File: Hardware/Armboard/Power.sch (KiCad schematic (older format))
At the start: 13 parts, among them J1 Test_Point, U1 LM2576D2TR4

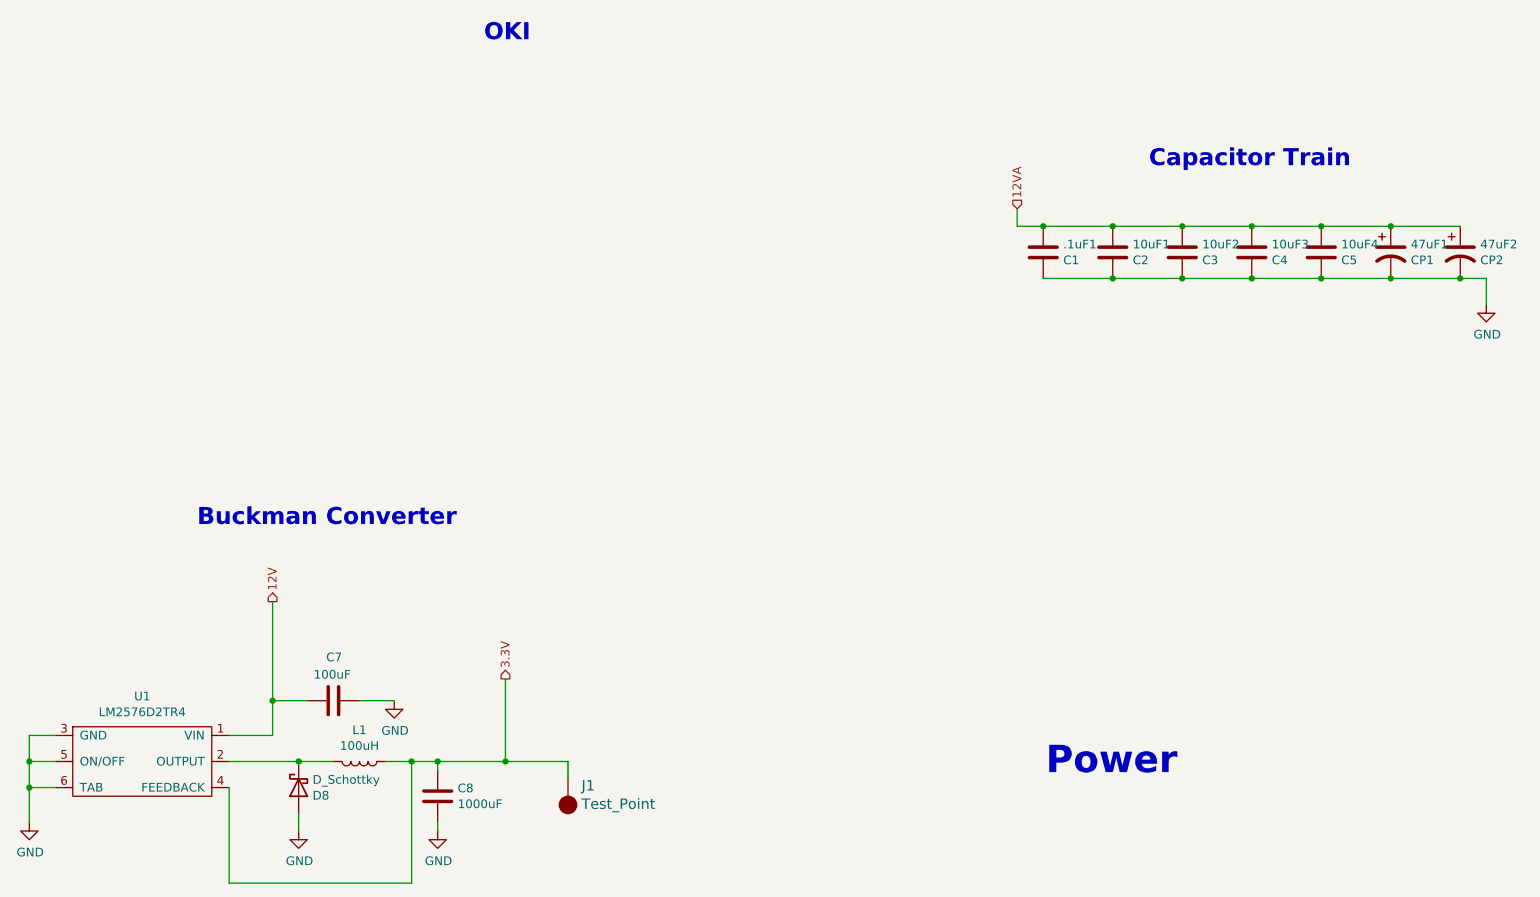
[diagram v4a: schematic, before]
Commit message: Replaced buckman with OKI
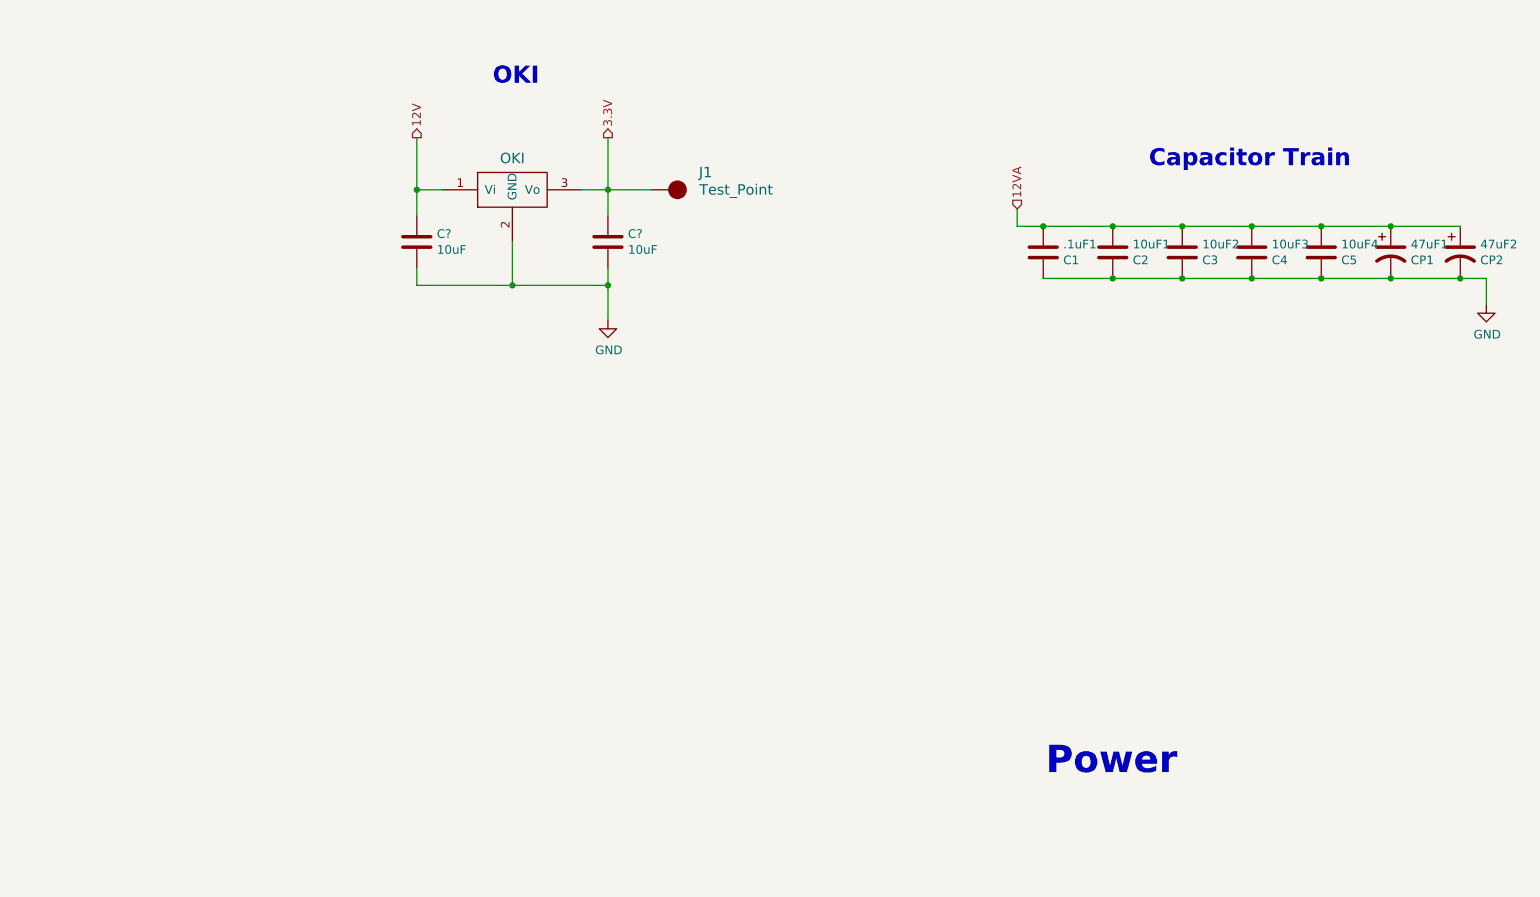
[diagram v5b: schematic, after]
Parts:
- removed C7: 100uF, Capacitor_SMD:C_0603_1608Metric_Pad1.05x0.95mm_HandSolder, symbol Device:C
- removed C8: 1000uF, Capacitor_SMD:C_0603_1608Metric_Pad1.05x0.95mm_HandSolder, symbol Device:C
- removed D8: D_Schottky, Diode_THT:D_DO-201AD_P15.24mm_Horizontal, symbol Device:D_Schottky
- removed L1: 100uH, Inductor_SMD:L_0603_1608Metric_Pad1.05x0.95mm_HandSolder, symbol Device:L
- removed U1: LM2576D2TR4, MRDT_Devices:LM2576, symbol Armboard-rescue:LM2576D2TR4-MRDT_Devices-Armboard-rescue
- added C? (x2): 10uF, symbol Device:C
- added U?: OKI, symbol MRDT_Devices:OKI
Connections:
- net 12V: now also C?.1, U?.1 (Vi)
- net 3.3V: now also C?.1, U?.3 (Vo)
- net GND: now also C?.2, C?.2, U?.2 (GND)
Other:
- note removed: "Buckman Converter"
- moved on the sheet: J1
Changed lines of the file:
@@
 $EndComp
 $Comp
-L Armboard-rescue:LM2576D2TR4-MRDT_Devices-Armboard-rescue U1
-U 1 1 5F74DE4A
-P 1420 7090
-F 0 "U1" H 1420 7515 50  0000 C CNN
-F 1 "LM2576D2TR4" H 1420 7424 50  0000 C CNN
-F 2 "MRDT_Devices:LM2576" H 1420 7540 50  0001 C CNN
-F 3 "https://www.mouser.com/datasheet/2/308/LM2576_D-1810688.pdf" H 1420 7540 50  0001 C CNN
-	1    1420 7090
+L Armboard-rescue:Test_Point-MRDT_Connectors-Armboard-rescue J1
+U 1 1 5F75C39D
+P 4350 3750
+F 0 "J1" V 4250 4100 60  0000 R CNN
+F 1 "Test_Point" V 4350 4450 60  0000 R CNN
+F 2 "TestPoint:TestPoint_Pad_D2.5mm" H 4350 3700 60  0001 C CNN
+F 3 "" H 4350 3700 60  0001 C CNN
+	1    4350 3750
+	0    1    1    0
+$EndComp
+Text Notes 8375 3630 2    98   ~ 20
+Capacitor Train
+Text Notes 6620 7130 0    157  ~ 31
+Power
+Text HLabel 4100 3450 1    50   Output ~ 0
+3.3V
+Text HLabel 3000 3450 1    50   Output ~ 0
+12V
+Text HLabel 6455 3860 1    50   Input ~ 0
+12VA
+Text Notes 3705 3155 2    98   ~ 20
+OKI
+$Comp
+L MRDT_Devices:OKI U?
+U 1 1 5FB74CE4
+P 3350 3850
+F 0 "U?" H 3400 3800 60  0001 C CNN
+F 1 "OKI" H 3550 4131 60  0000 C CNN
+F 2 "" H 3150 3750 60  0001 C CNN
+F 3 "" H 3150 3750 60  0001 C CNN
+	1    3350 3850
 	1    0    0    -1
 $EndComp
 $Comp
-L power:GND #PWR08
-U 1 1 5F74E2A1
-P 770 7390
-F 0 "#PWR08" H 770 7140 50  0001 C CNN
-F 1 "GND" H 775 7217 50  0000 C CNN
-F 2 "" H 770 7390 50  0001 C CNN
-F 3 "" H 770 7390 50  0001 C CNN
-	1    770  7390
+L Device:C C?
+U 1 1 5FB77225
+P 3000 4050
+F 0 "C?" H 3115 4096 50  0000 L CNN
+F 1 "10uF" H 3115 4005 50  0000 L CNN
+F 2 "" H 3038 3900 50  0001 C CNN
+F 3 "~" H 3000 4050 50  0001 C CNN
+	1    3000 4050
+	1    0    0    -1
+$EndComp
+$Comp
+L Device:C C?
+U 1 1 5FB780BA
+P 4100 4050
+F 0 "C?" H 4215 4096 50  0000 L CNN
+F 1 "10uF" H 4215 4005 50  0000 L CNN
+F 2 "" H 4138 3900 50  0001 C CNN
+F 3 "~" H 4100 4050 50  0001 C CNN
+	1    4100 4050
+	1    0    0    -1
+$EndComp
+$Comp
+L power:GND #PWR?
+U 1 1 5FB785A8
+P 4100 4500
+F 0 "#PWR?" H 4100 4250 50  0001 C CNN
+F 1 "GND" H 4105 4327 50  0000 C CNN
+F 2 "" H 4100 4500 50  0001 C CNN
+F 3 "" H 4100 4500 50  0001 C CNN
+	1    4100 4500
 	1    0    0    -1
 $EndComp
 Wire Wire Line
-	920  6890 770  6890
+	3000 4200 3000 4300
 Wire Wire Line
-	920  7040 770  7040
+	3000 4300 3550 4300
 Wire Wire Line
-	770  6890 770  7040
-Connection ~ 770  7040
+	4100 4300 4100 4200
+Connection ~ 4100 4300
 Wire Wire Line
-	920  7190 770  7190
+	4100 4300 4100 4500
 Wire Wire Line
-	770  7040 770  7190
-Connection ~ 770  7190
+	3000 3900 3000 3750
 Wire Wire Line
-	770  7190 770  7390
+	3000 3750 3150 3750
 Wire Wire Line
-	1920 6890 2170 6890
+	3550 4050 3550 4300
+Connection ~ 3550 4300
 Wire Wire Line
-	2170 6890 2170 6690
-$Comp
-L Device:C C8
-U 1 1 5F750C41
-P 3120 7240
-F 0 "C8" H 3235 7286 50  0000 L CNN
-F 1 "1000uF" H 3235 7195 50  0000 L CNN
-F 2 "Capacitor_SMD:C_0603_1608Metric_Pad1.05x0.95mm_HandSolder" H 3158 7090 50  0001 C CNN
-F 3 "~" H 3120 7240 50  0001 C CNN
-	1    3120 7240
-	1    0    0    -1
-$EndComp
-$Comp
-L Device:C C7
-U 1 1 5F75145E
-P 2520 6690
-F 0 "C7" V 2770 6640 50  0000 L CNN
-F 1 "100uF" V 2670 6590 50  0000 L CNN
-F 2 "Capacitor_SMD:C_0603_1608Metric_Pad1.05x0.95mm_HandSolder" H 2558 6540 50  0001 C CNN
-F 3 "~" H 2520 6690 50  0001 C CNN
-	1    2520 6690
-	0    -1   -1   0
-$EndComp
+	3550 4300 4100 4300
 Wire Wire Line
-	2170 6690 2370 6690
-Connection ~ 2170 6690
-$Comp
-L power:GND #PWR010
-U 1 1 5F75423C
-P 2870 6690
-F 0 "#PWR010" H 2870 6440 50  0001 C CNN
-F 1 "GND" H 2875 6517 50  0000 C CNN
-F 2 "" H 2870 6690 50  0001 C CNN
-F 3 "" H 2870 6690 50  0001 C CNN
-	1    2870 6690
-	1    0    0    -1
-$EndComp
+	4100 3750 4100 3900
 Wire Wire Line
-	2670 6690 2870 6690
-$Comp
-L Device:L L1
-U 1 1 5F755388
-P 2670 7040
-F 0 "L1" V 2489 7040 50  0000 C CNN
-F 1 "100uH" V 2580 7040 50  0000 C CNN
-F 2 "Inductor_SMD:L_0603_1608Metric_Pad1.05x0.95mm_HandSolder" H 2670 7040 50  0001 C CNN
-F 3 "~" H 2670 7040 50  0001 C CNN
-	1    2670 7040
-	0    1    1    0
-$EndComp
-$Comp
-L power:GND #PWR09
-U 1 1 5F75782E
-P 2320 7440
-F 0 "#PWR09" H 2320 7190 50  0001 C CNN
-F 1 "GND" H 2325 7267 50  0000 C CNN
-F 2 "" H 2320 7440 50  0001 C CNN
-F 3 "" H 2320 7440 50  0001 C CNN
-	1    2320 7440
-	1    0    0    -1
-$EndComp
+	3950 3750 4100 3750
 Wire Wire Line
-	2320 7340 2320 7440
+	3000 3750 3000 3450
+Connection ~ 3000 3750
 Wire Wire Line
-	2820 7040 2970 7040
+	4100 3750 4100 3450
+Connection ~ 4100 3750
 Wire Wire Line
-	3120 7040 3120 7090
-Wire Wire Line
-	1920 7190 1920 7740
-Wire Wire Line
-	1920 7740 2970 7740
-Wire Wire Line
-	2970 7740 2970 7040
-Connection ~ 2970 7040
-Wire Wire Line
-	2970 7040 3120 7040
-$Comp
-L power:GND #PWR011
-U 1 1 5F75A24F
-P 3120 7440
-F 0 "#PWR011" H 3120 7190 50  0001 C CNN
-F 1 "GND" H 3125 7267 50  0000 C CNN
-F 2 "" H 3120 7440 50  0001 C CNN
-F 3 "" H 3120 7440 50  0001 C CNN
-	1    3120 7440
-	1    0    0    -1
-$EndComp
-Wire Wire Line
-	3120 7440 3120 7390
-$Comp
-L Armboard-rescue:Test_Point-MRDT_Connectors-Armboard-rescue J1
-U 1 1 5F75C39D
-P 3870 7140
-F 0 "J1" H 3792 7179 60  0000 R CNN
-F 1 "Test_Point" H 3792 7285 60  0000 R CNN
-F 2 "TestPoint:TestPoint_Pad_D2.5mm" H 3870 7090 60  0001 C CNN
-F 3 "" H 3870 7090 60  0001 C CNN
-	1    3870 7140
-	-1   0    0    1
-$EndComp
-Wire Wire Line
-	3870 7040 3870 7140
-Connection ~ 3120 7040
-Text Notes 3230 5695 2    98   ~ 20
-Buckman Converter
-Text Notes 8375 3630 2    98   ~ 20
-Capacitor Train
-$Comp
-L Device:D_Schottky D8
-U 1 1 5F83C9A2
-P 2320 7190
-F 0 "D8" V 2366 7110 50  0000 R CNN
-F 1 "D_Schottky" V 2275 7110 50  0000 R CNN
-F 2 "Diode_THT:D_DO-201AD_P15.24mm_Horizontal" H 2320 7190 50  0001 C CNN
-F 3 "~" H 2320 7190 50  0001 C CNN
-	1    2320 7190
-	0    -1   1    0
-$EndComp
-Wire Wire Line
-	1920 7040 2320 7040
-Connection ~ 2320 7040
-Wire Wire Line
-	2320 7040 2520 7040
-Text Notes 6620 7130 0    157  ~ 31
-Power
-Text HLabel 3510 6565 1    50   Output ~ 0
-3.3V
-Text HLabel 2170 6120 1    50   Output ~ 0
-12V
-Wire Wire Line
-	2170 6120 2170 6690
-Wire Wire Line
-	3120 7040 3510 7040
-Wire Wire Line
-	3510 6565 3510 7040
-Connection ~ 3510 7040
-Wire Wire Line
-	3510 7040 3870 7040
-Text HLabel 6455 3860 1    50   Input ~ 0
-12VA
-Text Notes 3655 2905 2    98   ~ 20
-OKI
+	4100 3750 4350 3750
 $EndSCHEMATC

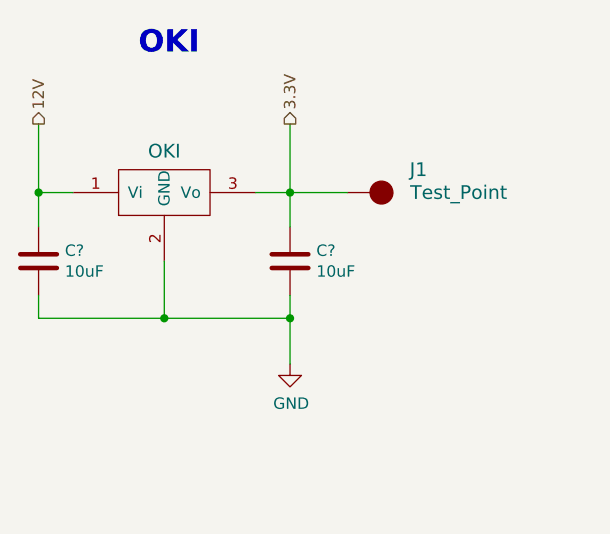
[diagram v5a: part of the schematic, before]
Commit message: Updated footprints, generated new netlist
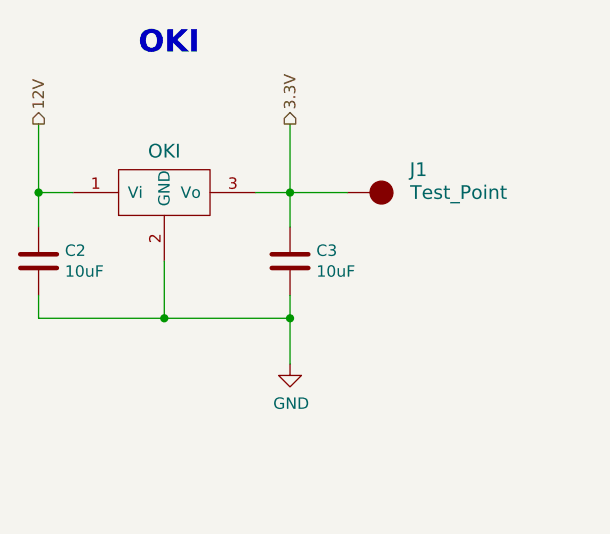
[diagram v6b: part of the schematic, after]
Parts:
- C2, C3: renamed from C?; footprint (none) -> Capacitor_SMD:C_0603_1608Metric_Pad1.05x0.95mm_HandSolder
- J1: footprint TestPoint:TestPoint_Pad_D2.5mm -> TestPoint:TestPoint_Pad_3.0x3.0mm
- U1: renamed from U?; footprint (none) -> MRDT_Devices:OKI_Horizontal
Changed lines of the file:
@@
 F 0 "J1" V 4250 4100 60  0000 R CNN
 F 1 "Test_Point" V 4350 4450 60  0000 R CNN
-F 2 "TestPoint:TestPoint_Pad_D2.5mm" H 4350 3700 60  0001 C CNN
+F 2 "TestPoint:TestPoint_Pad_3.0x3.0mm" H 4350 3700 60  0001 C CNN
 F 3 "" H 4350 3700 60  0001 C CNN
 	1    4350 3750
@@
 OKI
 $Comp
-L MRDT_Devices:OKI U?
+L MRDT_Devices:OKI U1
 U 1 1 5FB74CE4
 P 3350 3850
-F 0 "U?" H 3400 3800 60  0001 C CNN
+F 0 "U1" H 3400 3800 60  0001 C CNN
 F 1 "OKI" H 3550 4131 60  0000 C CNN
-F 2 "" H 3150 3750 60  0001 C CNN
+F 2 "MRDT_Devices:OKI_Horizontal" H 3150 3750 60  0001 C CNN
 F 3 "" H 3150 3750 60  0001 C CNN
 	1    3350 3850
@@
 $EndComp
 $Comp
-L Device:C C?
+L Device:C C2
 U 1 1 5FB77225
 P 3000 4050
-F 0 "C?" H 3115 4096 50  0000 L CNN
+F 0 "C2" H 3115 4096 50  0000 L CNN
 F 1 "10uF" H 3115 4005 50  0000 L CNN
-F 2 "" H 3038 3900 50  0001 C CNN
+F 2 "Capacitor_SMD:C_0603_1608Metric_Pad1.05x0.95mm_HandSolder" H 3038 3900 50  0001 C CNN
 F 3 "~" H 3000 4050 50  0001 C CNN
 	1    3000 4050
@@
 $EndComp
 $Comp
-L Device:C C?
+L Device:C C3
 U 1 1 5FB780BA
 P 4100 4050
-F 0 "C?" H 4215 4096 50  0000 L CNN
+F 0 "C3" H 4215 4096 50  0000 L CNN
 F 1 "10uF" H 4215 4005 50  0000 L CNN
-F 2 "" H 4138 3900 50  0001 C CNN
+F 2 "Capacitor_SMD:C_0603_1608Metric_Pad1.05x0.95mm_HandSolder" H 4138 3900 50  0001 C CNN
 F 3 "~" H 4100 4050 50  0001 C CNN
 	1    4100 4050
@@
 $EndComp
 $Comp
-L power:GND #PWR?
+L power:GND #PWR01
 U 1 1 5FB785A8
 P 4100 4500
-F 0 "#PWR?" H 4100 4250 50  0001 C CNN
+F 0 "#PWR01" H 4100 4250 50  0001 C CNN
 F 1 "GND" H 4105 4327 50  0000 C CNN
 F 2 "" H 4100 4500 50  0001 C CNN

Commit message: Added silkscreen designs
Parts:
- 47uF1, 47uF2: footprint Capacitor_SMD:CP_Elec_5x5.4 -> Capacitor_THT:CP_Radial_D5.0mm_P2.50mm
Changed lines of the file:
@@
 F 0 "47uF1" H 8720 4156 50  0000 L CNN
 F 1 "CP1" H 8720 4065 50  0000 L CNN
-F 2 "Capacitor_SMD:CP_Elec_5x5.4" H 8605 4110 50  0001 C CNN
+F 2 "Capacitor_THT:CP_Radial_D5.0mm_P2.50mm" H 8605 4110 50  0001 C CNN
 F 3 "~" H 8605 4110 50  0001 C CNN
 	1    8605 4110
@@
 F 0 "47uF2" H 9120 4156 50  0000 L CNN
 F 1 "CP2" H 9120 4065 50  0000 L CNN
-F 2 "Capacitor_SMD:CP_Elec_5x5.4" H 9005 4110 50  0001 C CNN
+F 2 "Capacitor_THT:CP_Radial_D5.0mm_P2.50mm" H 9005 4110 50  0001 C CNN
 F 3 "~" H 9005 4110 50  0001 C CNN
 	1    9005 4110

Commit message: Fixed some library issues and moved Gerbs to Manufacturing folder
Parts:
- .1uF1, 10uF1, 10uF2, 10uF3, 10uF4, C2, C3: footprint Capacitor_SMD:C_0603_1608Metric_Pad1.05x0.95mm_HandSolder -> Capacitor_SMD:C_0603_1608Metric_Pad1.08x0.95mm_HandSolder
- 47uF1, 47uF2: symbol Device:CP1 -> Device:C_Polarized_US
- J1: symbol Armboard-rescue:Test_Point-MRDT_Connectors-Armboard-rescue -> MRDT_Connectors:Test_Point
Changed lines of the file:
@@
 EESchema Schematic File Version 4
+LIBS:Armboard-cache
 EELAYER 30 0
 EELAYER END
@@
 F 0 ".1uF1" H 6720 4156 50  0000 L CNN
 F 1 "C1" H 6720 4065 50  0000 L CNN
-F 2 "Capacitor_SMD:C_0603_1608Metric_Pad1.05x0.95mm_HandSolder" H 6643 3960 50  0001 C CNN
+F 2 "Capacitor_SMD:C_0603_1608Metric_Pad1.08x0.95mm_HandSolder" H 6643 3960 50  0001 C CNN
 F 3 "~" H 6605 4110 50  0001 C CNN
 	1    6605 4110
@@
 F 0 "10uF1" H 7120 4156 50  0000 L CNN
 F 1 "C2" H 7120 4065 50  0000 L CNN
-F 2 "Capacitor_SMD:C_0603_1608Metric_Pad1.05x0.95mm_HandSolder" H 7043 3960 50  0001 C CNN
+F 2 "Capacitor_SMD:C_0603_1608Metric_Pad1.08x0.95mm_HandSolder" H 7043 3960 50  0001 C CNN
 F 3 "~" H 7005 4110 50  0001 C CNN
 	1    7005 4110
@@
 F 0 "10uF2" H 7520 4156 50  0000 L CNN
 F 1 "C3" H 7520 4065 50  0000 L CNN
-F 2 "Capacitor_SMD:C_0603_1608Metric_Pad1.05x0.95mm_HandSolder" H 7443 3960 50  0001 C CNN
+F 2 "Capacitor_SMD:C_0603_1608Metric_Pad1.08x0.95mm_HandSolder" H 7443 3960 50  0001 C CNN
 F 3 "~" H 7405 4110 50  0001 C CNN
 	1    7405 4110
@@
 F 0 "10uF3" H 7920 4156 50  0000 L CNN
 F 1 "C4" H 7920 4065 50  0000 L CNN
-F 2 "Capacitor_SMD:C_0603_1608Metric_Pad1.05x0.95mm_HandSolder" H 7843 3960 50  0001 C CNN
+F 2 "Capacitor_SMD:C_0603_1608Metric_Pad1.08x0.95mm_HandSolder" H 7843 3960 50  0001 C CNN
 F 3 "~" H 7805 4110 50  0001 C CNN
 	1    7805 4110
@@
 F 0 "10uF4" H 8320 4156 50  0000 L CNN
 F 1 "C5" H 8320 4065 50  0000 L CNN
-F 2 "Capacitor_SMD:C_0603_1608Metric_Pad1.05x0.95mm_HandSolder" H 8243 3960 50  0001 C CNN
+F 2 "Capacitor_SMD:C_0603_1608Metric_Pad1.08x0.95mm_HandSolder" H 8243 3960 50  0001 C CNN
 F 3 "~" H 8205 4110 50  0001 C CNN
 	1    8205 4110
-	1    0    0    -1
-$EndComp
-$Comp
-L Device:CP1 47uF1
-U 1 1 5F67C954
-P 8605 4110
-F 0 "47uF1" H 8720 4156 50  0000 L CNN
-F 1 "CP1" H 8720 4065 50  0000 L CNN
-F 2 "Capacitor_THT:CP_Radial_D5.0mm_P2.50mm" H 8605 4110 50  0001 C CNN
-F 3 "~" H 8605 4110 50  0001 C CNN
-	1    8605 4110
-	1    0    0    -1
-$EndComp
-$Comp
-L Device:CP1 47uF2
-U 1 1 5F67D4A0
-P 9005 4110
-F 0 "47uF2" H 9120 4156 50  0000 L CNN
-F 1 "CP2" H 9120 4065 50  0000 L CNN
-F 2 "Capacitor_THT:CP_Radial_D5.0mm_P2.50mm" H 9005 4110 50  0001 C CNN
-F 3 "~" H 9005 4110 50  0001 C CNN
-	1    9005 4110
 	1    0    0    -1
 $EndComp
@@
 $EndComp
 $Comp
-L Armboard-rescue:Test_Point-MRDT_Connectors-Armboard-rescue J1
+L MRDT_Connectors:Test_Point J1
 U 1 1 5F75C39D
 P 4350 3750
+AR Path="/5F75C39D" Ref="J1"  Part="1"
+AR Path="/5F67ABAC/5F75C39D" Ref="J1"  Part="1"
 F 0 "J1" V 4250 4100 60  0000 R CNN
 F 1 "Test_Point" V 4350 4450 60  0000 R CNN
@@
 F 0 "C2" H 3115 4096 50  0000 L CNN
 F 1 "10uF" H 3115 4005 50  0000 L CNN
-F 2 "Capacitor_SMD:C_0603_1608Metric_Pad1.05x0.95mm_HandSolder" H 3038 3900 50  0001 C CNN
+F 2 "Capacitor_SMD:C_0603_1608Metric_Pad1.08x0.95mm_HandSolder" H 3038 3900 50  0001 C CNN
 F 3 "~" H 3000 4050 50  0001 C CNN
 	1    3000 4050
@@
 F 0 "C3" H 4215 4096 50  0000 L CNN
 F 1 "10uF" H 4215 4005 50  0000 L CNN
-F 2 "Capacitor_SMD:C_0603_1608Metric_Pad1.05x0.95mm_HandSolder" H 4138 3900 50  0001 C CNN
+F 2 "Capacitor_SMD:C_0603_1608Metric_Pad1.08x0.95mm_HandSolder" H 4138 3900 50  0001 C CNN
 F 3 "~" H 4100 4050 50  0001 C CNN
 	1    4100 4050
@@
 Wire Wire Line
 	4100 3750 4350 3750
+$Comp
+L Device:C_Polarized_US 47uF2
+U 1 1 5F67D4A0
+P 9005 4110
+AR Path="/5F67D4A0" Ref="47uF2"  Part="1"
+AR Path="/5F67ABAC/5F67D4A0" Ref="47uF2"  Part="1"
+F 0 "47uF2" H 9120 4156 50  0000 L CNN
+F 1 "CP2" H 9120 4065 50  0000 L CNN
+F 2 "Capacitor_THT:CP_Radial_D5.0mm_P2.50mm" H 9005 4110 50  0001 C CNN
+F 3 "~" H 9005 4110 50  0001 C CNN
+	1    9005 4110
+	1    0    0    -1
+$EndComp
+$Comp
+L Device:C_Polarized_US 47uF1
+U 1 1 5F67C954
+P 8605 4110
+AR Path="/5F67C954" Ref="47uF1"  Part="1"
+AR Path="/5F67ABAC/5F67C954" Ref="47uF1"  Part="1"
+F 0 "47uF1" H 8720 4156 50  0000 L CNN
+F 1 "CP1" H 8720 4065 50  0000 L CNN
+F 2 "Capacitor_THT:CP_Radial_D5.0mm_P2.50mm" H 8605 4110 50  0001 C CNN
+F 3 "~" H 8605 4110 50  0001 C CNN
+	1    8605 4110
+	1    0    0    -1
+$EndComp
 $EndSCHEMATC
